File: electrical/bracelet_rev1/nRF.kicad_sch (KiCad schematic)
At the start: 21 parts, among them U1 nRF54L10-QFXX, Y1 Crystal_GND24

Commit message: Many schematic updates
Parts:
- added AE1: Antenna, symbol Device:Antenna
- added C24: 10uF, symbol Device:C
- added J2: Conn_01x04_Pin, symbol Connector:Conn_01x04_Pin
- added R13: 10k, symbol Device:R
- added SW1: SW_Push, symbol Switch:SW_Push
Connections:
- net GND: now also C24.2, J2.4 (Pin_4), SW1.2
- net NRESET: now also C24.1, R13.1, SW1.1
- net SWDCLK: now also J2.3 (Pin_3)
- net SWDIO: now also J2.2 (Pin_2)
- net at C12.1, L4.2: now also AE1.1 (A)
- net VDD renamed 1V8
- net 1V8: now also J2.1 (Pin_1), R13.2
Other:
- note added: "Note: Want this to be a right angle connector to save space"
- moved on the sheet: C1, C10, C11, C12, C13, C2, C3, C4, C5, C6, C7, C8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

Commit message: Mostly finihsed hopefully but still needs clean up anyway
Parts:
- added R18, R19: R, symbol Device:R
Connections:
- net 1V8: now also R18.1, R19.1
- net WS2812_DIN: now reaches U1.13 (P2.02)
- net POX_INT: now reaches U1.2 (P1.01)
- net SDA: now reaches U1.3 (P1.02)
- net SDA: now also R19.2
- net IMU_INT2: now reaches U1.37 (P1.09)
- net SCL: now reaches U1.4 (P1.03)
- net SCL: now also R18.2
- net IMU_INT1: now reaches U1.6 (P1.05)
- net CURR_SENSE: now reaches U1.7 (P1.06)
- net VBATT_SENSE: now reaches U1.8 (P1.07)
- net BUZZER: now reaches U1.9 (P1.08)

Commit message: May updates
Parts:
- added D5: LED, symbol Device:LED
- added R20: 1k, symbol Device:R
- R18, R19: value R -> 4.7k
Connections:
- net GND: now also D5.1 (K)
- net USER_LED: now reaches U1.42 (P1.14)
- net USER_LED: now also R20.1
- new net: D5.2 (A), R20.2
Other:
- moved on the sheet: J2

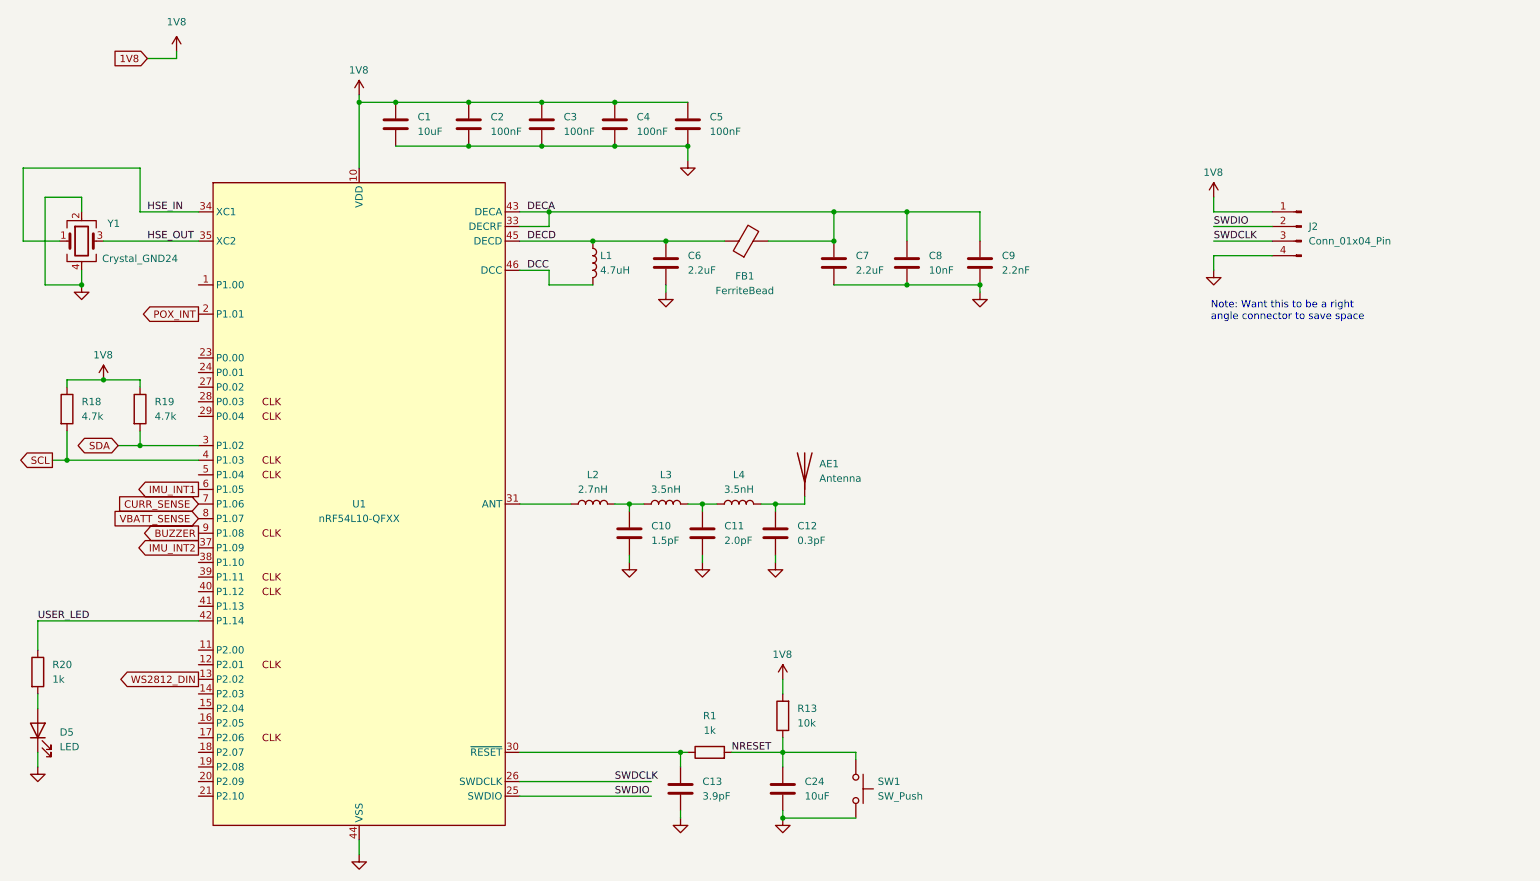
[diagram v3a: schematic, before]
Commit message: Redo component numbers
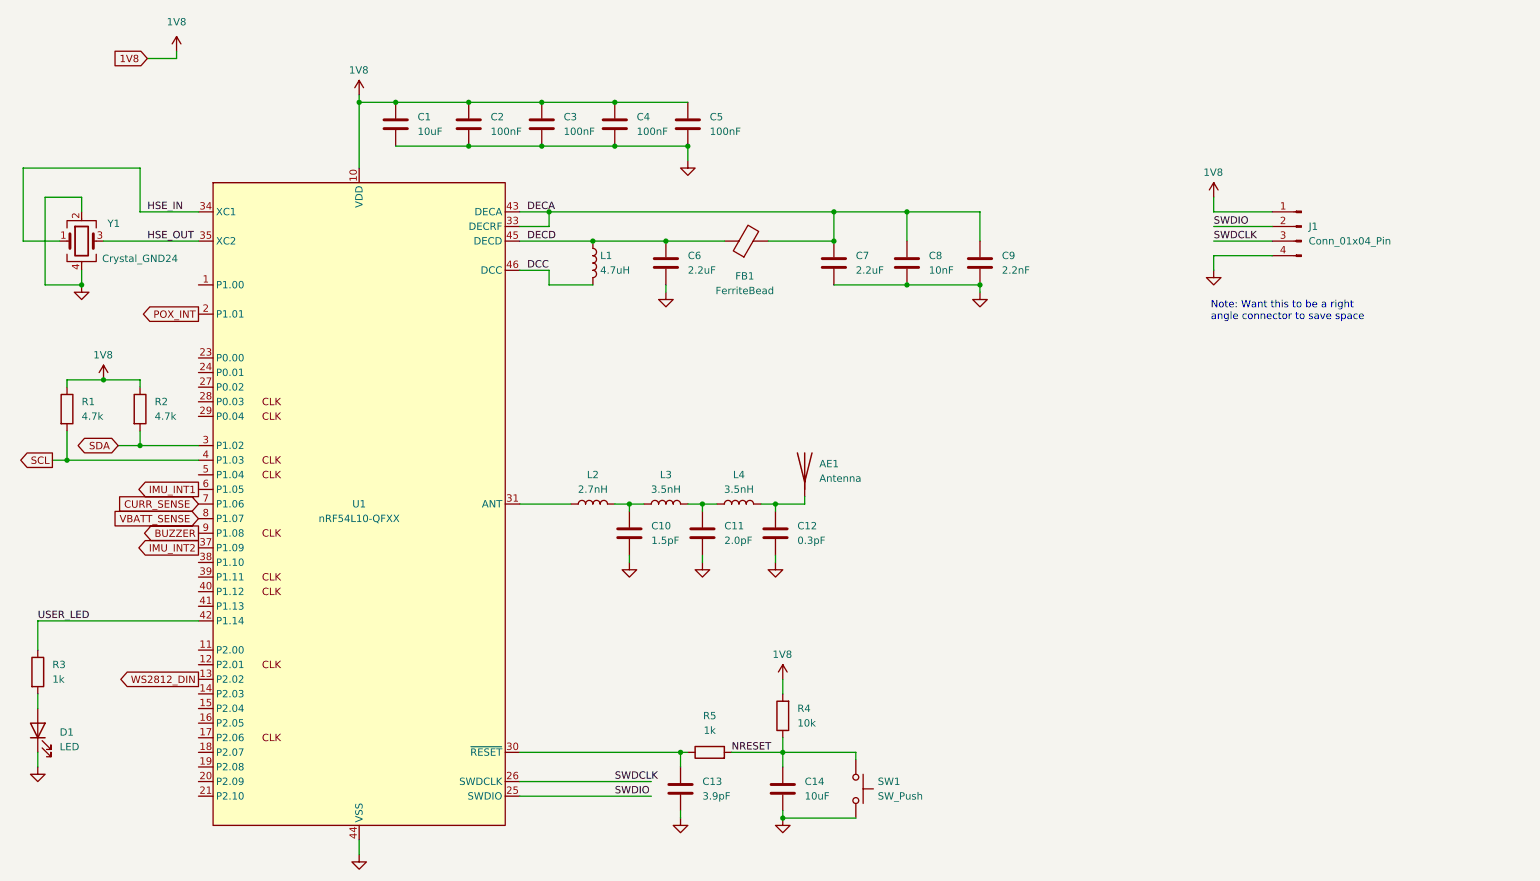
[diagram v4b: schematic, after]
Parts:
- renumbered C24 to C14, D5 to D1, J2 to J1, R18 to R1, R19 to R2, R20 to R3, R13 to R4, R1 to R5
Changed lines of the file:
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@@
 		(on_board yes)
 		(dnp no)
-		(property "Reference" "#PWR048"
+		(property "Reference" "#PWR?"
 			(at 153.67 135.89 0)
 			(effects
@@
 			(project "bracelet_rev1"
 				(path "/2a7dd2e8-59c9-4d04-9427-958ca4ea7daa/ad786af7-ff00-44f4-8204-9aee6ad471a6"
-					(reference "#PWR048")
+					(reference "#PWR?")
 					(unit 1)
 				)
@@
 		(dnp no)
 		(fields_autoplaced yes)
-		(property "Reference" "R13"
+		(property "Reference" "R4"
 			(at 156.21 137.1599 0)
 			(effects
@@
 			(project "bracelet_rev1"
 				(path "/2a7dd2e8-59c9-4d04-9427-958ca4ea7daa/ad786af7-ff00-44f4-8204-9aee6ad471a6"
-					(reference "R13")
+					(reference "R4")
 					(unit 1)
 				)
@@
 		(dnp no)
 		(fields_autoplaced yes)
-		(property "Reference" "R1"
+		(property "Reference" "R5"
 			(at 140.97 138.43 90)
 			(effects
@@
 			(project "bracelet_rev1"
 				(path "/2a7dd2e8-59c9-4d04-9427-958ca4ea7daa/ad786af7-ff00-44f4-8204-9aee6ad471a6"
-					(reference "R1")
+					(reference "R5")
 					(unit 1)
 				)
@@
 		(dnp no)
 		(fields_autoplaced yes)
-		(property "Reference" "#PWR04"
+		(property "Reference" "#PWR?"
 			(at 133.35 71.12 0)
 			(effects
@@
 			(project "bracelet_rev1"
 				(path "/2a7dd2e8-59c9-4d04-9427-958ca4ea7daa/ad786af7-ff00-44f4-8204-9aee6ad471a6"
-					(reference "#PWR04")
+					(reference "#PWR?")
 					(unit 1)
 				)
@@
 		(dnp no)
 		(fields_autoplaced yes)
-		(property "Reference" "R19"
+		(property "Reference" "R2"
 			(at 44.45 83.8199 0)
 			(effects
@@
 			(project "bracelet_rev1"
 				(path "/2a7dd2e8-59c9-4d04-9427-958ca4ea7daa/ad786af7-ff00-44f4-8204-9aee6ad471a6"
-					(reference "R19")
+					(reference "R2")
 					(unit 1)
 				)
@@
 		(dnp no)
 		(fields_autoplaced yes)
-		(property "Reference" "#PWR01"
+		(property "Reference" "#PWR?"
 			(at 80.01 168.91 0)
 			(effects
@@
 			(project "bracelet_rev1"
 				(path "/2a7dd2e8-59c9-4d04-9427-958ca4ea7daa/ad786af7-ff00-44f4-8204-9aee6ad471a6"
-					(reference "#PWR01")
+					(reference "#PWR?")
 					(unit 1)
 				)
@@
 		(dnp no)
 		(fields_autoplaced yes)
-		(property "Reference" "#PWR07"
+		(property "Reference" "#PWR?"
 			(at 127 118.11 0)
 			(effects
@@
 			(project "bracelet_rev1"
 				(path "/2a7dd2e8-59c9-4d04-9427-958ca4ea7daa/ad786af7-ff00-44f4-8204-9aee6ad471a6"
-					(reference "#PWR07")
+					(reference "#PWR?")
 					(unit 1)
 				)
@@
 		(dnp no)
 		(fields_autoplaced yes)
-		(property "Reference" "C24"
+		(property "Reference" "C14"
 			(at 157.48 149.8599 0)
 			(effects
@@
 			(project "bracelet_rev1"
 				(path "/2a7dd2e8-59c9-4d04-9427-958ca4ea7daa/ad786af7-ff00-44f4-8204-9aee6ad471a6"
-					(reference "C24")
+					(reference "C14")
 					(unit 1)
 				)
@@
 		(on_board yes)
 		(dnp no)
-		(property "Reference" "#PWR011"
+		(property "Reference" "#PWR?"
 			(at 228.6 52.07 0)
 			(effects
@@
 			(project "bracelet_rev1"
 				(path "/2a7dd2e8-59c9-4d04-9427-958ca4ea7daa/ad786af7-ff00-44f4-8204-9aee6ad471a6"
-					(reference "#PWR011")
+					(reference "#PWR?")
 					(unit 1)
 				)
@@
 		(dnp no)
 		(fields_autoplaced yes)
-		(property "Reference" "#PWR010"
+		(property "Reference" "#PWR?"
 			(at 135.89 162.56 0)
 			(effects
@@
 			(project "bracelet_rev1"
 				(path "/2a7dd2e8-59c9-4d04-9427-958ca4ea7daa/ad786af7-ff00-44f4-8204-9aee6ad471a6"
-					(reference "#PWR010")
+					(reference "#PWR?")
 					(unit 1)
 				)
@@
 		(dnp no)
 		(fields_autoplaced yes)
-		(property "Reference" "#PWR013"
+		(property "Reference" "#PWR?"
 			(at 228.6 67.31 0)
 			(effects
@@
 			(project "bracelet_rev1"
 				(path "/2a7dd2e8-59c9-4d04-9427-958ca4ea7daa/ad786af7-ff00-44f4-8204-9aee6ad471a6"
-					(reference "#PWR013")
+					(reference "#PWR?")
 					(unit 1)
 				)
@@
 		(dnp no)
 		(fields_autoplaced yes)
-		(property "Reference" "#PWR06"
+		(property "Reference" "#PWR?"
 			(at 31.75 69.85 0)
 			(effects
@@
 			(project "bracelet_rev1"
 				(path "/2a7dd2e8-59c9-4d04-9427-958ca4ea7daa/ad786af7-ff00-44f4-8204-9aee6ad471a6"
-					(reference "#PWR06")
+					(reference "#PWR?")
 					(unit 1)
 				)
@@
 		(dnp no)
 		(fields_autoplaced yes)
-		(property "Reference" "#PWR074"
+		(property "Reference" "#PWR?"
 			(at 24.13 153.67 0)
 			(effects
@@
 			(project "bracelet_rev1"
 				(path "/2a7dd2e8-59c9-4d04-9427-958ca4ea7daa/ad786af7-ff00-44f4-8204-9aee6ad471a6"
-					(reference "#PWR074")
+					(reference "#PWR?")
 					(unit 1)
 				)
@@
 		(dnp no)
 		(fields_autoplaced yes)
-		(property "Reference" "J2"
+		(property "Reference" "J1"
 			(at 245.11 53.3399 0)
 			(effects
@@
 			(project ""
 				(path "/2a7dd2e8-59c9-4d04-9427-958ca4ea7daa/ad786af7-ff00-44f4-8204-9aee6ad471a6"
-					(reference "J2")
+					(reference "J1")
 					(unit 1)
 				)
@@
 		(dnp no)
 		(fields_autoplaced yes)
-		(property "Reference" "D5"
+		(property "Reference" "D1"
 			(at 27.94 141.2874 90)
 			(effects
@@
 			(project ""
 				(path "/2a7dd2e8-59c9-4d04-9427-958ca4ea7daa/ad786af7-ff00-44f4-8204-9aee6ad471a6"
-					(reference "D5")
+					(reference "D1")
 					(unit 1)
 				)
@@
 		(dnp no)
 		(fields_autoplaced yes)
-		(property "Reference" "#PWR08"
+		(property "Reference" "#PWR?"
 			(at 139.7 118.11 0)
 			(effects
@@
 			(project "bracelet_rev1"
 				(path "/2a7dd2e8-59c9-4d04-9427-958ca4ea7daa/ad786af7-ff00-44f4-8204-9aee6ad471a6"
-					(reference "#PWR08")
+					(reference "#PWR?")
 					(unit 1)
 				)
@@
 		(dnp no)
 		(fields_autoplaced yes)
-		(property "Reference" "#PWR03"
+		(property "Reference" "#PWR?"
 			(at 137.16 48.26 0)
 			(effects
@@
 			(project "bracelet_rev1"
 				(path "/2a7dd2e8-59c9-4d04-9427-958ca4ea7daa/ad786af7-ff00-44f4-8204-9aee6ad471a6"
-					(reference "#PWR03")
+					(reference "#PWR?")
 					(unit 1)
 				)
@@
 		(dnp no)
 		(fields_autoplaced yes)
-		(property "Reference" "#PWR09"
+		(property "Reference" "#PWR?"
 			(at 152.4 118.11 0)
 			(effects
@@
 			(project "bracelet_rev1"
 				(path "/2a7dd2e8-59c9-4d04-9427-958ca4ea7daa/ad786af7-ff00-44f4-8204-9aee6ad471a6"
-					(reference "#PWR09")
+					(reference "#PWR?")
 					(unit 1)
 				)
@@
 		(on_board yes)
 		(dnp no)
-		(property "Reference" "#PWR026"
+		(property "Reference" "#PWR?"
 			(at 35.56 83.82 0)
 			(effects
@@
 			(project "bracelet_rev1"
 				(path "/2a7dd2e8-59c9-4d04-9427-958ca4ea7daa/ad786af7-ff00-44f4-8204-9aee6ad471a6"
-					(reference "#PWR026")
+					(reference "#PWR?")
 					(unit 1)
 				)
@@
 		(dnp no)
 		(fields_autoplaced yes)
-		(property "Reference" "#PWR042"
+		(property "Reference" "#PWR?"
 			(at 48.26 26.67 0)
 			(effects
@@
 			(project "bracelet_rev1"
 				(path "/2a7dd2e8-59c9-4d04-9427-958ca4ea7daa/ad786af7-ff00-44f4-8204-9aee6ad471a6"
-					(reference "#PWR042")
+					(reference "#PWR?")
 					(unit 1)
 				)
@@
 		(dnp no)
 		(fields_autoplaced yes)
-		(property "Reference" "#PWR049"
+		(property "Reference" "#PWR?"
 			(at 153.67 162.56 0)
 			(effects
@@
 			(project "bracelet_rev1"
 				(path "/2a7dd2e8-59c9-4d04-9427-958ca4ea7daa/ad786af7-ff00-44f4-8204-9aee6ad471a6"
-					(reference "#PWR049")
+					(reference "#PWR?")
 					(unit 1)
 				)
@@
 		(dnp no)
 		(fields_autoplaced yes)
-		(property "Reference" "R18"
+		(property "Reference" "R1"
 			(at 31.75 83.8199 0)
 			(effects
@@
 			(project ""
 				(path "/2a7dd2e8-59c9-4d04-9427-958ca4ea7daa/ad786af7-ff00-44f4-8204-9aee6ad471a6"
-					(reference "R18")
+					(reference "R1")
 					(unit 1)
 				)
@@
 		(dnp no)
 		(fields_autoplaced yes)
-		(property "Reference" "R20"
+		(property "Reference" "R3"
 			(at 26.67 129.5399 0)
 			(effects
@@
 			(project "bracelet_rev1"
 				(path "/2a7dd2e8-59c9-4d04-9427-958ca4ea7daa/ad786af7-ff00-44f4-8204-9aee6ad471a6"
-					(reference "R20")
+					(reference "R3")
 					(unit 1)
 				)
@@
 		(dnp no)
 		(fields_autoplaced yes)
-		(property "Reference" "#PWR05"
+		(property "Reference" "#PWR?"
 			(at 187.96 71.12 0)
 			(effects
@@
 			(project "bracelet_rev1"
 				(path "/2a7dd2e8-59c9-4d04-9427-958ca4ea7daa/ad786af7-ff00-44f4-8204-9aee6ad471a6"
-					(reference "#PWR05")
+					(reference "#PWR?")
 					(unit 1)
 				)
@@
 		(on_board yes)
 		(dnp no)
-		(property "Reference" "#PWR02"
+		(property "Reference" "#PWR?"
 			(at 80.01 34.29 0)
 			(effects
@@
 			(project "bracelet_rev1"
 				(path "/2a7dd2e8-59c9-4d04-9427-958ca4ea7daa/ad786af7-ff00-44f4-8204-9aee6ad471a6"
-					(reference "#PWR02")
+					(reference "#PWR?")
 					(unit 1)
 				)

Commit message: Updated more things
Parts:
- added D5: LED, symbol Device:LED
- added J4: Conn_01x04_Pin, symbol Connector:Conn_01x04_Pin
- added R22: 1k, symbol Device:R
- added R23: 200, symbol Device:R
- added U8: ~, symbol LSF0102V8:LSF0102TA8-7
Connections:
- net 1V8: now also U8.2 (Vref_A)
- net BUZZER: now also U1.1 (P1.00); no longer U1.9 (P1.08)
- net GND: now also D5.1 (K), J4.4 (Pin_4), U8.1 (GND)
- net SCL: now also U8.3 (A1)
- net SDA: now also U8.4 (A2)
- net SPI_CLK: now reaches U1.12 (P2.01)
- net n70_SW_CTRL0: now reaches U1.14 (P2.03)
- net SPI_MISO: now reaches U1.15 (P2.04)
- net SPI_CS: now reaches U1.16 (P2.05)
- net n70_HOST_IRQ: now reaches U1.17 (P2.06)
- net n70_COEX_STATUS0: now reaches U1.18 (P2.07)
- net n70_COEX_STATUS1: now reaches U1.19 (P2.08)
- net n70_COEX_REQ: now reaches U1.20 (P2.09)
- net n70_COEX_GRANT: now reaches U1.21 (P2.10)
- net USER_LED2: now reaches U1.39 (P1.11)
- net USER_LED2: now also R22.1
- net USER_BUTTON: now reaches U1.41 (P1.13)
- net WS2812_DIN renamed SPI_MOSI
- new net: R23.1, U8.8 (EN)
- new net: D5.2 (A), R22.2
- new net 3V3: J4.1 (Pin_1), R23.2, U8.7 (Vref_B)
- new net SCL_3V3: J4.2 (Pin_2), U8.6 (B1)
- new net SDA_3V3: J4.3 (Pin_3), U8.5 (B2)
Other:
- moved on the sheet: AE1, C1, C10, C11, C12, C13, C14, C2, C3, C4, C5, C6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

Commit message: More schematic stuff
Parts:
- C1, C10, C11, C12, C13, C14, C2, C3, C4, C5, C6, C7, C8, C9: footprint (none) -> Capacitor_SMD:C_0603_1608Metric_Pad1.08x0.95mm_HandSolder
- D1, D5: footprint (none) -> LED_SMD:LED_0603_1608Metric_Pad1.05x0.95mm_HandSolder
- FB1, L1, L2, L3, L4: footprint (none) -> Inductor_SMD:L_0603_1608Metric_Pad1.05x0.95mm_HandSolder
- J1, J4: footprint (none) -> Connector_PinHeader_2.54mm:PinHeader_1x04_P2.54mm_Vertical
- R1, R2, R3, R4, R5: footprint (none) -> Resistor_SMD:R_0603_1608Metric_Pad0.98x0.95mm_HandSolder
- R22, R23: footprint (none) -> Resistor_SMD:R_0201_0603Metric_Pad0.64x0.40mm_HandSolder
- Y1: footprint (none) -> Crystal:Crystal_SMD_3225-4Pin_3.2x2.5mm_HandSoldering
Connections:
- net SCL: no longer U8.3 (A1)
- net SDA: no longer U8.4 (A2)
- net UART_TX: now reaches U1.23 (P0.00)
- net UART_TX: now also U8.3 (A1)
- net UART_RX: now reaches U1.24 (P0.01)
- net UART_RX: now also U8.4 (A2)
- net BMP_IT: now reaches U1.27 (P0.02)
- net SCL_3V3 renamed UART_TX_3V3
- net SDA_3V3 renamed UART_RX_3V3
- no-connect marks 0 -> 7
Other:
- moved on the sheet: J4, R23, U8
